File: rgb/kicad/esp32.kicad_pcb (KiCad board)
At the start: 2 copper layers, 90.2 x 49.6 mm, 72 parts, among them J1 5 / 12V, J10 W1, J11 +12V, J12 R2, J13 G2, J14 B2, J15 CONN FT232RL, J16 W2, J17 +12V, J18 R3, J19 G3, J2 +12V, J20 B3, J21 W3, J22 +12V, J23 R4, J24 G4, J25 B4, J26 W1, J3 R1, J4 G1, J5 hole, J6 hole, J7 hole, J8 hole, J9 B1, Q1 ZXMS6004, Q10 ZXMS6004, Q11 ZXMS6004, Q12 ZXMS6004, Q13 ZXMS6004, Q14 ZXMS6004, Q15 ZXMS6004, Q16 ZXMS6004, Q2 ZXMS6004, Q3 ZXMS6004, Q4 ZXMS6004, Q5 ZXMS6004, Q6 ZXMS6004, Q7 ZXMS6004, Q8 ZXMS6004, Q9 ZXMS6004, SW1 RESET, SW2 PROG, U1 ESP32-WROOM-32U, U2 MS5637, U3 Si7020-A20, U4 PCA9685PW, U5 ACT4088, U6 DS18B20, U8 TCS3400

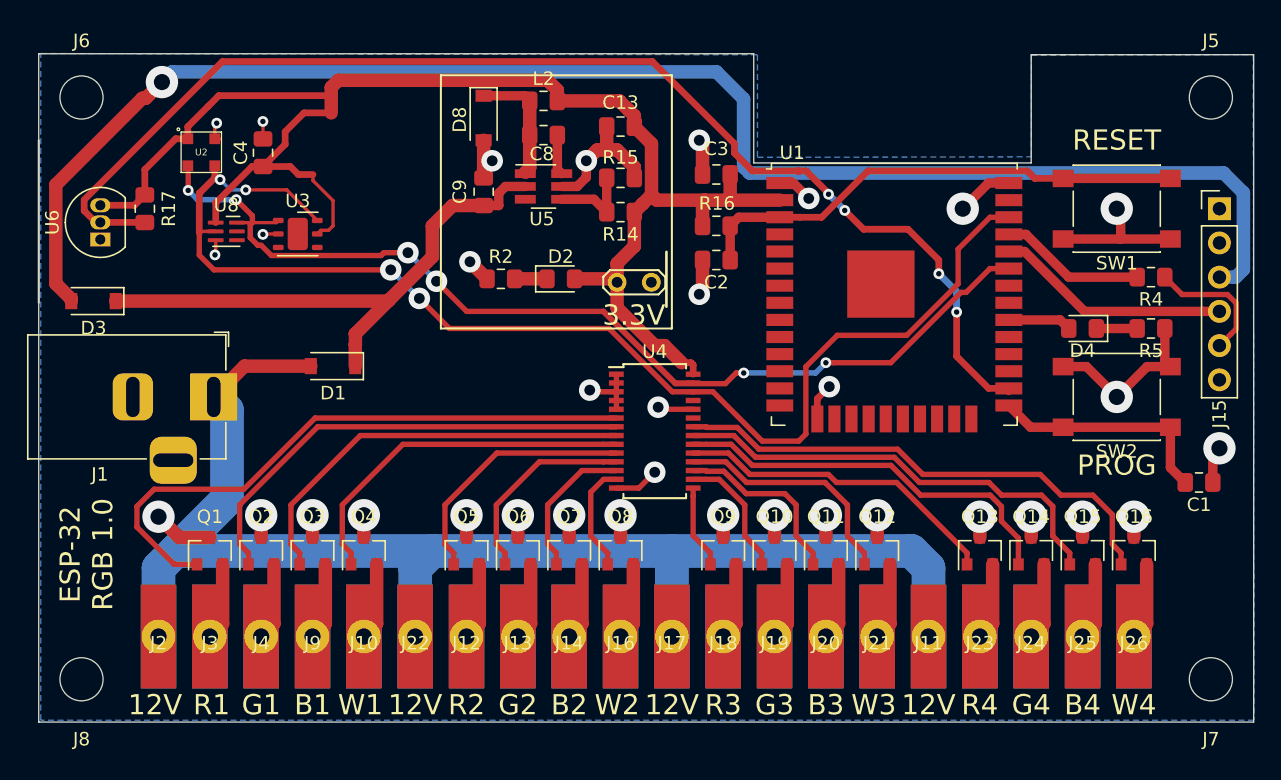
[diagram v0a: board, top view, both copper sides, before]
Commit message: fix(rgb): add DTR CSR, pullup IO0
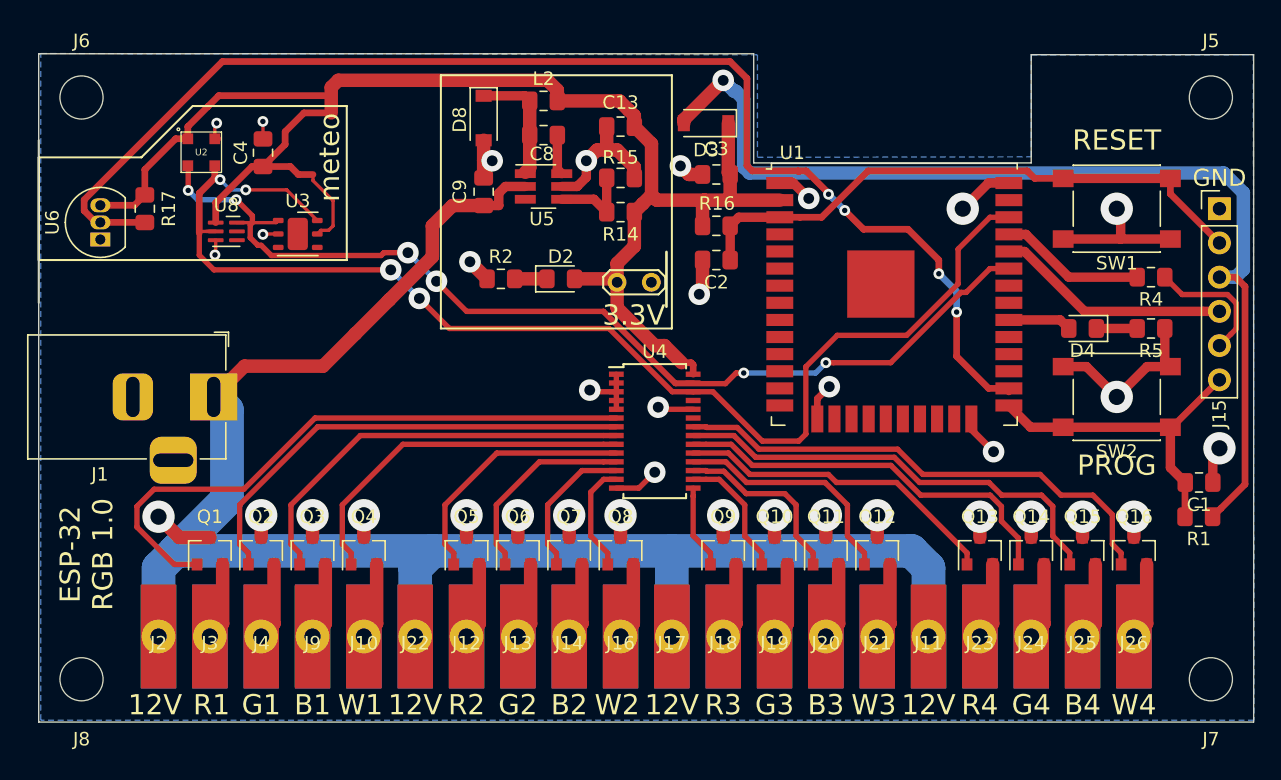
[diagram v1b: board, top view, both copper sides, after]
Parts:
- removed D1: D_Schottky, Diode_SMD:D_SOD-123
- added R1: 10k, Resistor_SMD:R_0805_2012Metric_Pad1.15x1.40mm_HandSolder, F.Cu at (166.1, 104.7)
- moved D3 47.3 mm to (129.6, 75.5)
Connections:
- C1 pad 2: /IO0 -> /DTR
- C2 pad 1: /RST -> /CTS
- C9 pad 1: /ACT4088-33/VIN -> +12V
- D3 pad 1: /ACT4088-33/VIN -> +3V3
- R16 pad 2: /RST -> /CTS
- SW1 pad 2: /RST -> /CTS
- SW2 pad 1: /IO0 -> /DTR
- U1 pad 24: Net-(U1-Pad24) -> GND
- U1 pad 25: /IO0 -> /DTR
- U1 pad 3: /RST -> /CTS
- U5 pad 2: /ACT4088-33/VIN -> +12V
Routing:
- net /CTS: track 0.00 -> 43.4 mm
- net /ACT4088-33/VIN: track 41.8 -> 0.00 mm
- net /VCC_FTDI: track 115.1 -> 77.4 mm
- net /RST: track 37.1 -> 0.00 mm
- net /DTR: track 0.00 -> 24.9 mm
- net +12V: track 103.2 -> 126.7 mm
- net /IO0: track 17.2 -> 0.00 mm
- net +3V3: track 113.6 -> 117.4 mm
- net ONE3: track 92.8 -> 96.2 mm
- net GND: track 101.1 -> 103.5 mm, vias 34 -> 35
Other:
- board text added: "GND"
- board text added: "meteo"
